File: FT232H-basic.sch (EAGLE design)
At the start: 27 parts, among them IC1 FT232H, U1 IP4220CZ6

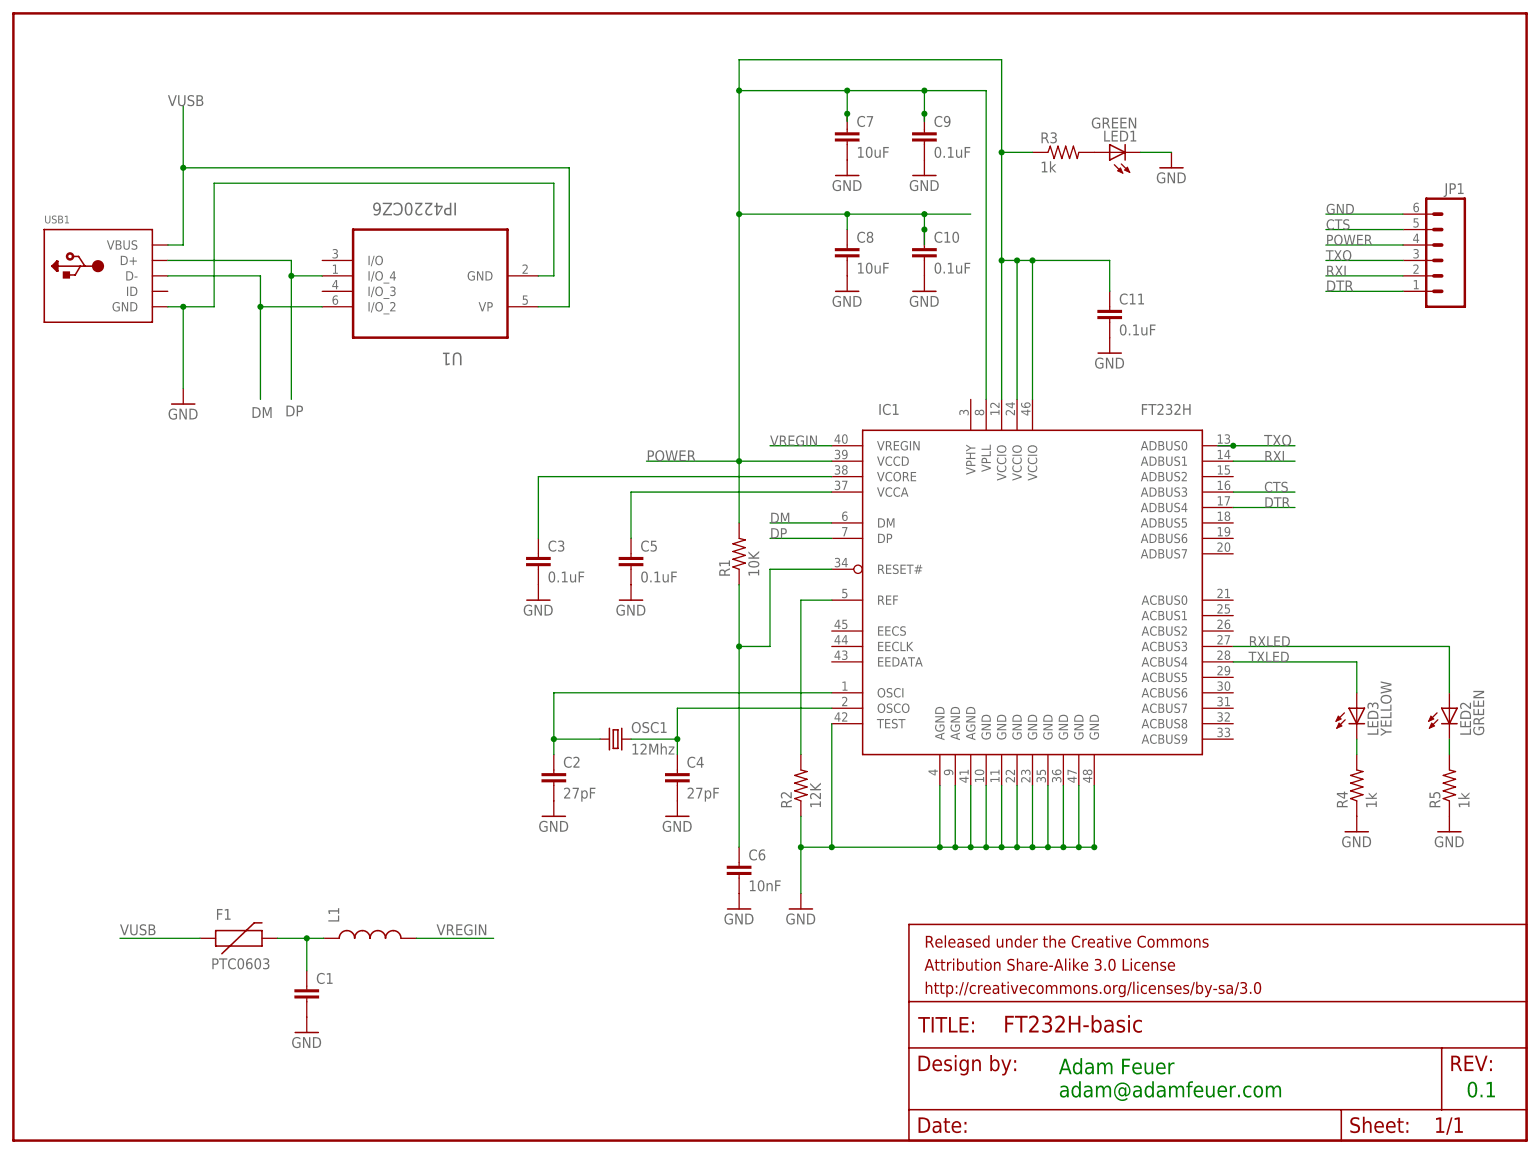
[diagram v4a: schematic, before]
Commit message: after v0.1 back from OSH Park: made part names larger, bumped version to 0.3
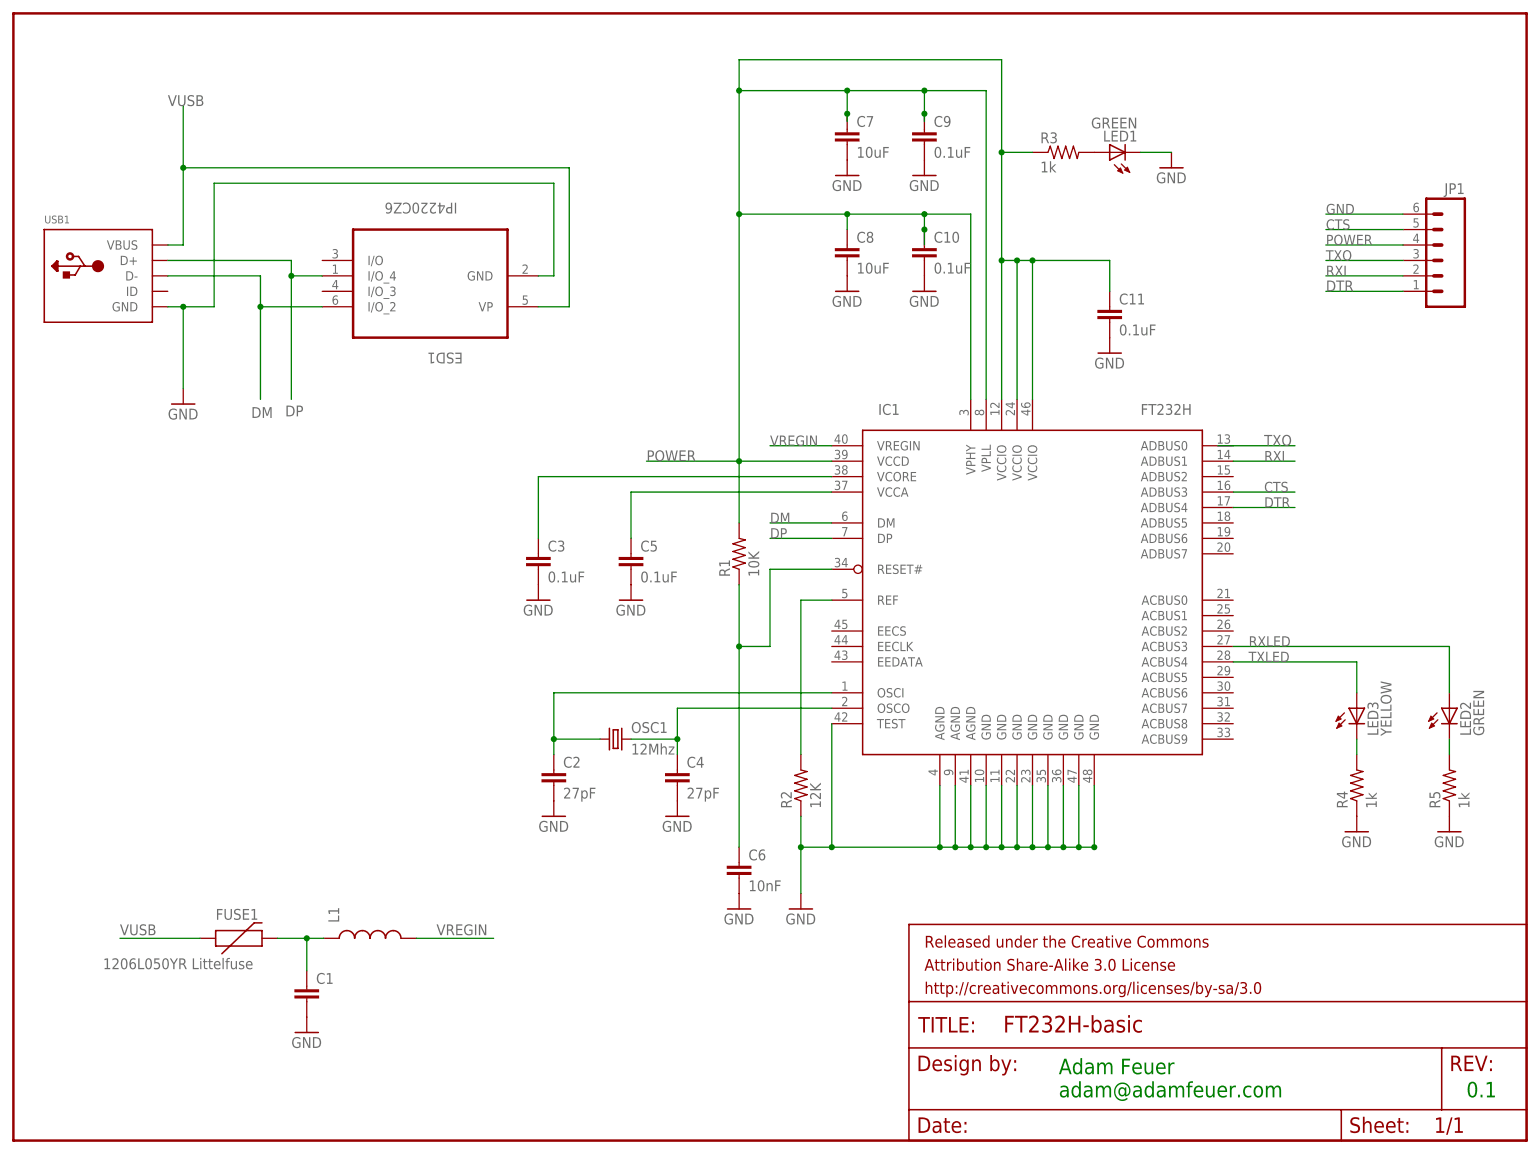
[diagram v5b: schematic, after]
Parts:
- FUSE1: value PTC0603 -> 1206L050YR Littelfuse
- renumbered F1 to FUSE1, U1 to ESD1
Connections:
- net POWER: now also IC1.VPHY
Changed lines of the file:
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@@
 <part name="OSC1" library="SparkFun-FreqCtrl" deviceset="CRYSTAL" device="5X3" value="12Mhz"/>
 <part name="FRAME1" library="SparkFun-Aesthetics" deviceset="FRAME-LETTER" device=""/>
-<part name="U1" library="NXP_By_element14_Batch_1" deviceset="IP4220CZ6" device=""/>
+<part name="ESD1" library="NXP_By_element14_Batch_1" deviceset="IP4220CZ6" device=""/>
 <part name="JP1" library="SparkFun-Connectors" deviceset="M06" device="SIP"/>
-<part name="F1" library="SparkFun-PowerIC" deviceset="PTC" device="0603"/>
+<part name="FUSE1" library="SparkFun-PowerIC" deviceset="PTC" device="0603" value="1206L050YR Littelfuse"/>
 <part name="L1" library="SparkFun-Passives" deviceset="INDUCTOR" device="0603"/>
 <part name="C1" library="SparkFun-Passives" deviceset="CAP" device="0603-CAP"/>
@@
 <instance part="FRAME1" gate="G$1" x="0" y="0"/>
 <instance part="FRAME1" gate="G$2" x="147.32" y="0"/>
-<instance part="U1" gate="A" x="68.58" y="137.16" rot="R180"/>
+<instance part="ESD1" gate="A" x="68.58" y="137.16" smashed="yes" rot="R180">
+<attribute name="NAME" x="73.9394" y="129.6162" size="1.778" layer="95" rot="SR180"/>
+<attribute name="VALUE" x="73.0504" y="154.2796" size="1.778" layer="96" rot="SR180"/>
+</instance>
 <instance part="JP1" gate="G$1" x="233.68" y="144.78" rot="MR0"/>
-<instance part="F1" gate="G$1" x="35.814" y="33.274"/>
+<instance part="FUSE1" gate="G$1" x="35.814" y="33.274" smashed="yes">
+<attribute name="NAME" x="33.274" y="36.322" size="1.778" layer="95"/>
+<attribute name="VALUE" x="14.732" y="28.194" size="1.778" layer="96"/>
+</instance>
 <instance part="L1" gate="G$1" x="58.674" y="33.274" rot="R90"/>
 <instance part="C1" gate="G$1" x="48.26" y="22.86"/>
@@
 <wire x1="33.02" y1="157.48" x2="88.9" y2="157.48" width="0.1524" layer="91"/>
 <wire x1="88.9" y1="157.48" x2="88.9" y2="142.24" width="0.1524" layer="91"/>
-<pinref part="U1" gate="A" pin="GND"/>
+<pinref part="ESD1" gate="A" pin="GND"/>
 <wire x1="88.9" y1="142.24" x2="86.36" y2="142.24" width="0.1524" layer="91"/>
 <junction x="27.94" y="137.16"/>
@@
 <wire x1="27.94" y1="160.02" x2="91.44" y2="160.02" width="0.1524" layer="91"/>
 <wire x1="91.44" y1="160.02" x2="91.44" y2="137.16" width="0.1524" layer="91"/>
-<pinref part="U1" gate="A" pin="VP"/>
+<pinref part="ESD1" gate="A" pin="VP"/>
 <wire x1="91.44" y1="137.16" x2="86.36" y2="137.16" width="0.1524" layer="91"/>
 <junction x="27.94" y="160.02"/>
@@
 <segment>
 <wire x1="17.526" y1="33.274" x2="30.734" y2="33.274" width="0.1524" layer="91"/>
-<pinref part="F1" gate="G$1" pin="1"/>
+<pinref part="FUSE1" gate="G$1" pin="1"/>
 <label x="17.526" y="33.782" size="1.778" layer="95"/>
 </segment>
@@
 <wire x1="25.4" y1="144.78" x2="45.72" y2="144.78" width="0.1524" layer="91"/>
 <wire x1="45.72" y1="144.78" x2="45.72" y2="142.24" width="0.1524" layer="91"/>
-<pinref part="U1" gate="A" pin="I/O_4"/>
+<pinref part="ESD1" gate="A" pin="I/O_4"/>
 <wire x1="45.72" y1="142.24" x2="50.8" y2="142.24" width="0.1524" layer="91"/>
 <wire x1="45.72" y1="142.24" x2="45.72" y2="121.92" width="0.1524" layer="91"/>
@@
 <wire x1="25.4" y1="142.24" x2="40.64" y2="142.24" width="0.1524" layer="91"/>
 <wire x1="40.64" y1="142.24" x2="40.64" y2="137.16" width="0.1524" layer="91"/>
-<pinref part="U1" gate="A" pin="I/O_2"/>
+<pinref part="ESD1" gate="A" pin="I/O_2"/>
 <wire x1="40.64" y1="137.16" x2="50.8" y2="137.16" width="0.1524" layer="91"/>
 <wire x1="40.64" y1="137.16" x2="40.64" y2="121.92" width="0.1524" layer="91"/>
@@
 <junction x="119.38" y="152.4"/>
 <junction x="162.56" y="162.56"/>
+<pinref part="IC1" gate="G$1" pin="VPHY"/>
+<wire x1="157.48" y1="121.92" x2="157.48" y2="152.4" width="0.1524" layer="91"/>
 </segment>
 </net>
@@
 <pinref part="IC1" gate="G$1" pin="ADBUS0"/>
 <wire x1="200.66" y1="114.3" x2="210.82" y2="114.3" width="0.1524" layer="91"/>
-<junction x="200.66" y="114.3"/>
 </segment>
 </net>
@@
 <net name="N$6" class="0">
 <segment>
-<pinref part="F1" gate="G$1" pin="2"/>
+<pinref part="FUSE1" gate="G$1" pin="2"/>
 <pinref part="L1" gate="G$1" pin="1"/>
 <wire x1="51.054" y1="33.274" x2="48.26" y2="33.274" width="0.1524" layer="91"/>

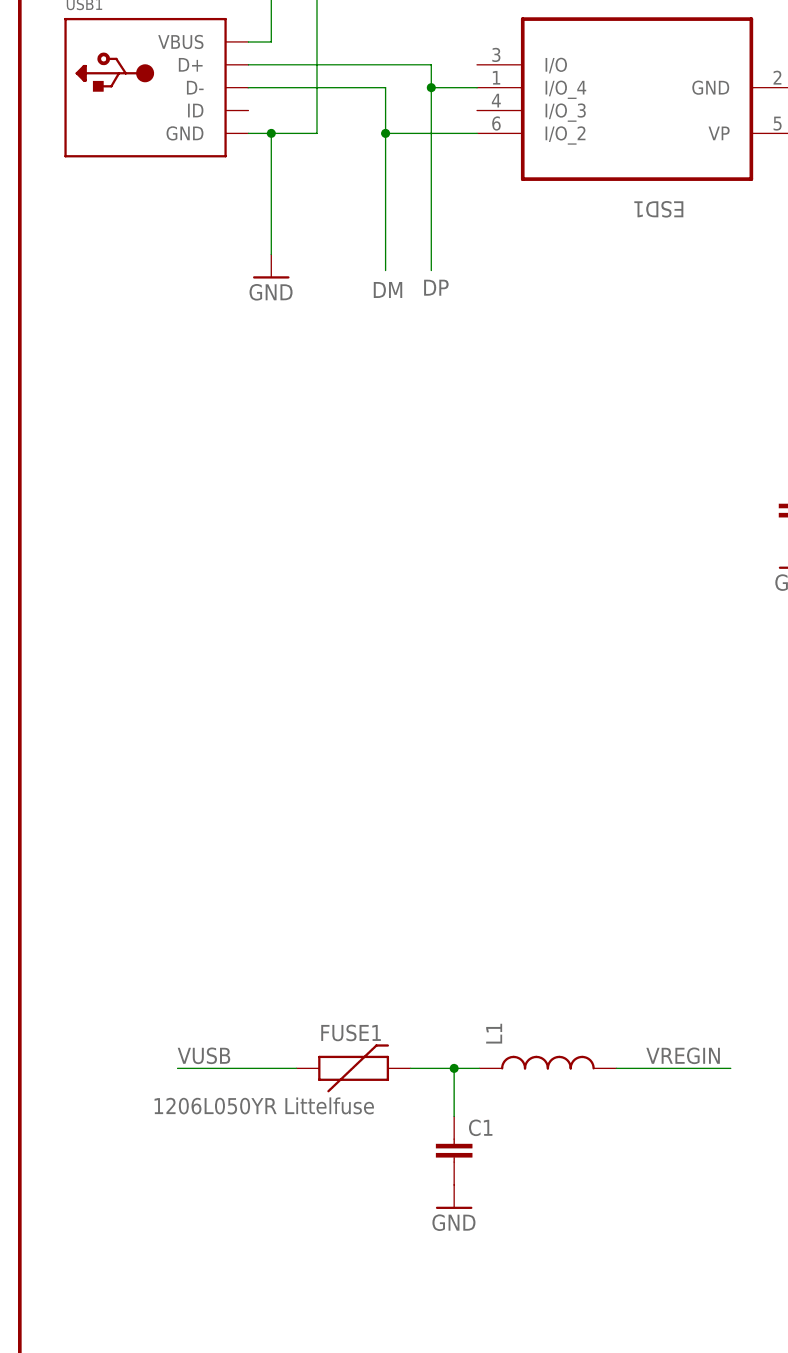
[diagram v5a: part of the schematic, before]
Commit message: board passes ERC
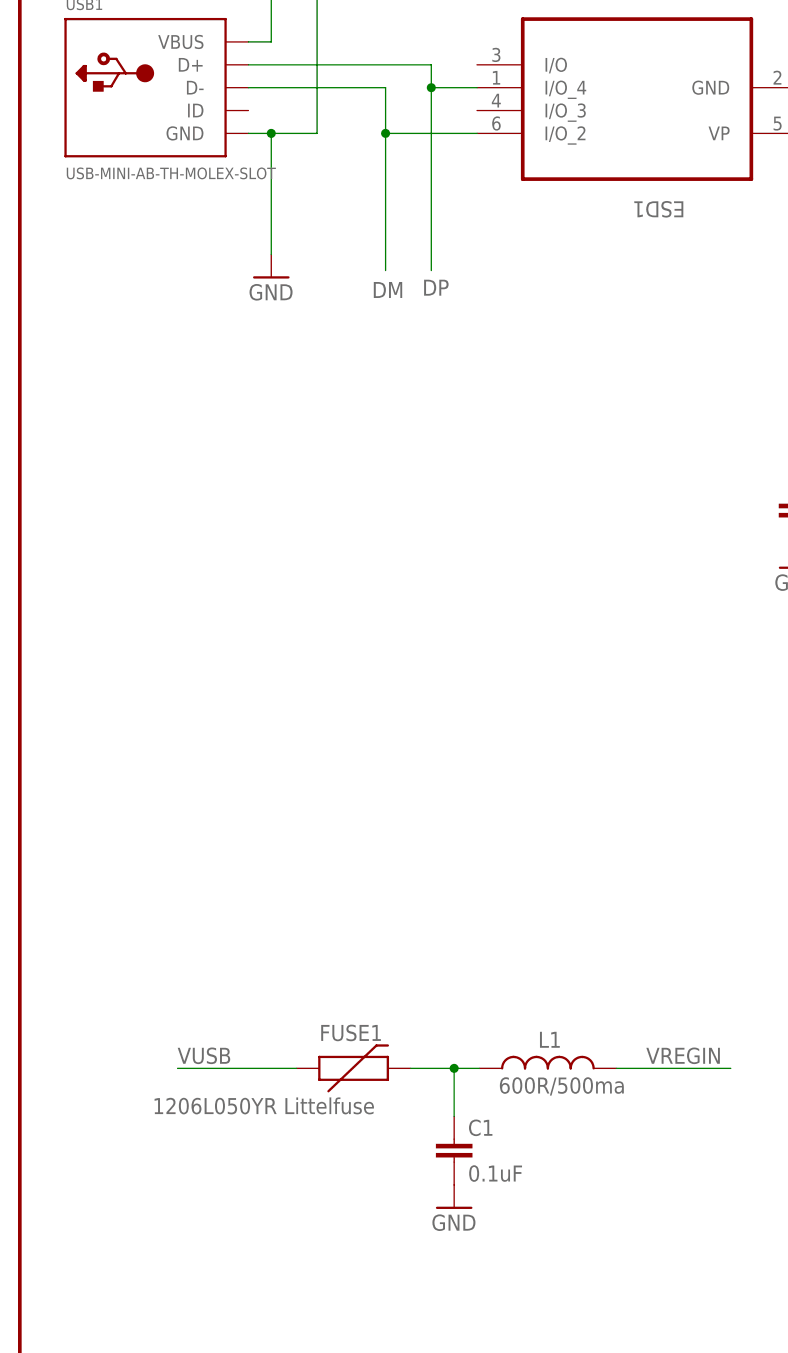
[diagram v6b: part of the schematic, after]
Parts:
- C1: value (none) -> 0.1uF
- L1: value (none) -> 600R/500ma
- USB1: value (none) -> USB-MINI-AB-TH-MOLEX-SLOT
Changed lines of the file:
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@@
 <part name="R3" library="SparkFun-Resistors" deviceset="1K-1%" device="" value="1k"/>
 <part name="GND12" library="SparkFun-Aesthetics" deviceset="GND" device=""/>
-<part name="USB1" library="USB-Mini-Molex" deviceset="USB-MINIB" device="TH-SLOT"/>
+<part name="USB1" library="USB-Mini-Molex" deviceset="USB-MINIB" device="TH-SLOT" value="USB-MINI-AB-TH-MOLEX-SLOT"/>
 <part name="GND14" library="SparkFun-Aesthetics" deviceset="GND" device=""/>
 <part name="LED2" library="SparkFun-LED" deviceset="LED-GREEN" device="0603" value="GREEN"/>
@@
 <part name="JP1" library="SparkFun-Connectors" deviceset="M06" device="SIP"/>
 <part name="FUSE1" library="SparkFun-PowerIC" deviceset="PTC" device="0603" value="1206L050YR Littelfuse"/>
-<part name="L1" library="SparkFun-Passives" deviceset="INDUCTOR" device="0603"/>
-<part name="C1" library="SparkFun-Passives" deviceset="CAP" device="0603-CAP"/>
+<part name="L1" library="SparkFun-Passives" deviceset="INDUCTOR" device="0603" value="600R/500ma"/>
+<part name="C1" library="SparkFun-Passives" deviceset="CAP" device="0603-CAP" value="0.1uF"/>
 <part name="GND13" library="SparkFun-Aesthetics" deviceset="GND" device=""/>
 </parts>
@@
 <attribute name="VALUE" x="14.732" y="28.194" size="1.778" layer="96"/>
 </instance>
-<instance part="L1" gate="G$1" x="58.674" y="33.274" rot="R90"/>
+<instance part="L1" gate="G$1" x="58.674" y="33.274" smashed="yes" rot="R90">
+<attribute name="NAME" x="60.198" y="37.338" size="1.778" layer="95" rot="R180"/>
+<attribute name="VALUE" x="67.31" y="32.258" size="1.778" layer="96" rot="R180"/>
+</instance>
 <instance part="C1" gate="G$1" x="48.26" y="22.86"/>
 <instance part="GND13" gate="1" x="48.26" y="17.78"/>
@@
 </sheet>
 </sheets>
+<errors>
+</errors>
 </schematic>
 </drawing>

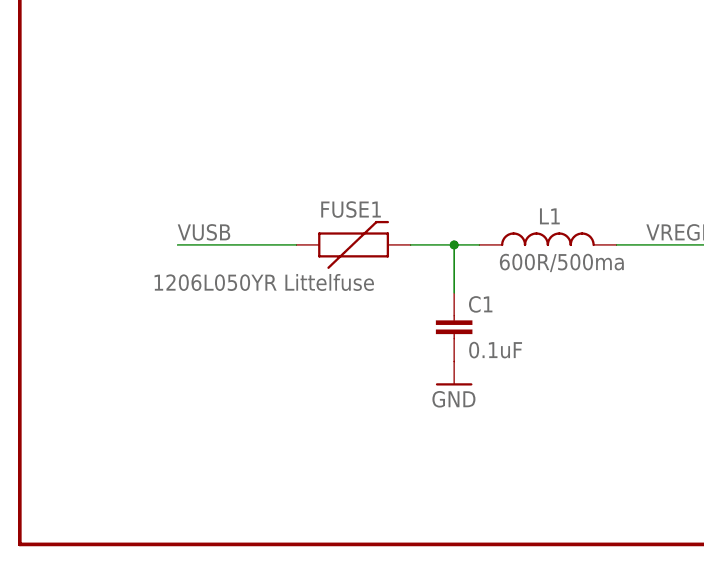
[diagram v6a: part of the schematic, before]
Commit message: updated schematic to reflect correct size 0603 of FUSE1
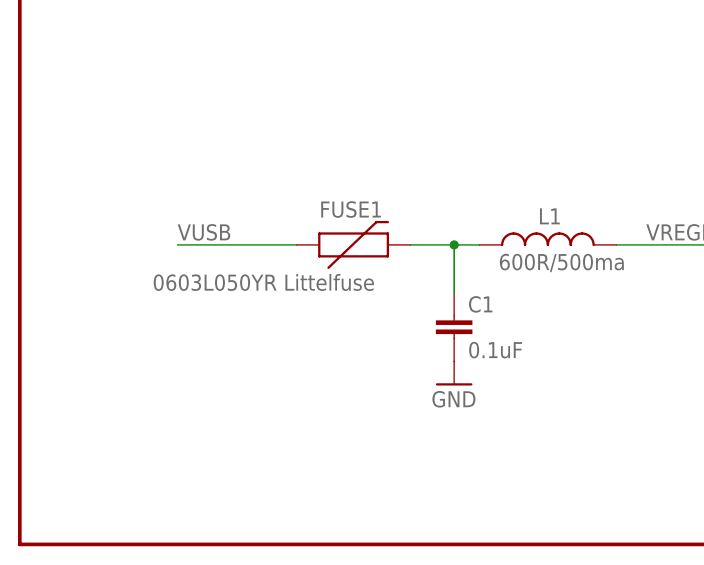
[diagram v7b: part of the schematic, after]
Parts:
- FUSE1: value 1206L050YR Littelfuse -> 0603L050YR Littelfuse
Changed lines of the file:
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@@
 <part name="ESD1" library="NXP_By_element14_Batch_1" deviceset="IP4220CZ6" device=""/>
 <part name="JP1" library="SparkFun-Connectors" deviceset="M06" device="SIP"/>
-<part name="FUSE1" library="SparkFun-PowerIC" deviceset="PTC" device="0603" value="1206L050YR Littelfuse"/>
+<part name="FUSE1" library="SparkFun-PowerIC" deviceset="PTC" device="0603" value="0603L050YR Littelfuse"/>
 <part name="L1" library="SparkFun-Passives" deviceset="INDUCTOR" device="0603" value="600R/500ma"/>
 <part name="C1" library="SparkFun-Passives" deviceset="CAP" device="0603-CAP" value="0.1uF"/>
